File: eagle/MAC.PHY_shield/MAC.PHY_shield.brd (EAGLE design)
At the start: 49.9 x 49.9 mm, 23 parts, among them IC1 ENC28J60, Q1 CSM-7X-DU

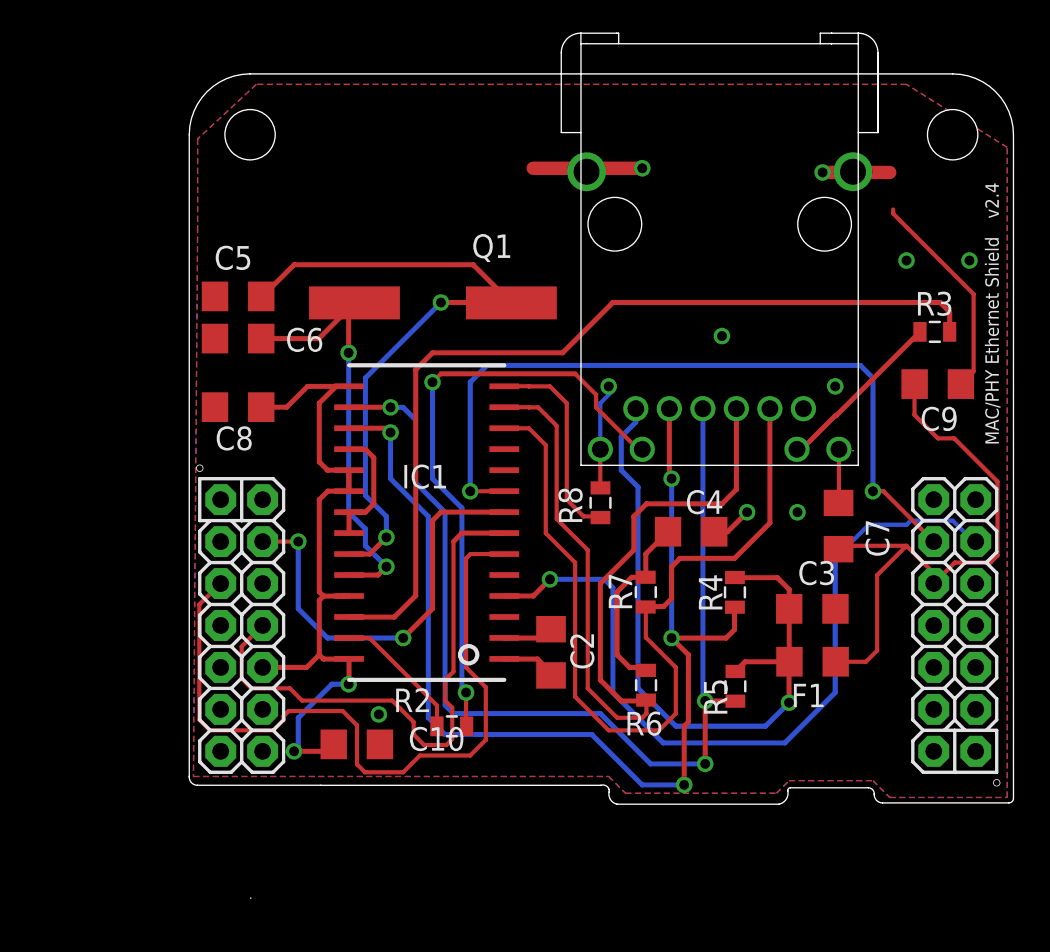
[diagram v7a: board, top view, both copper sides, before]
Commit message: Sent out boards to itead, last minute changes included.
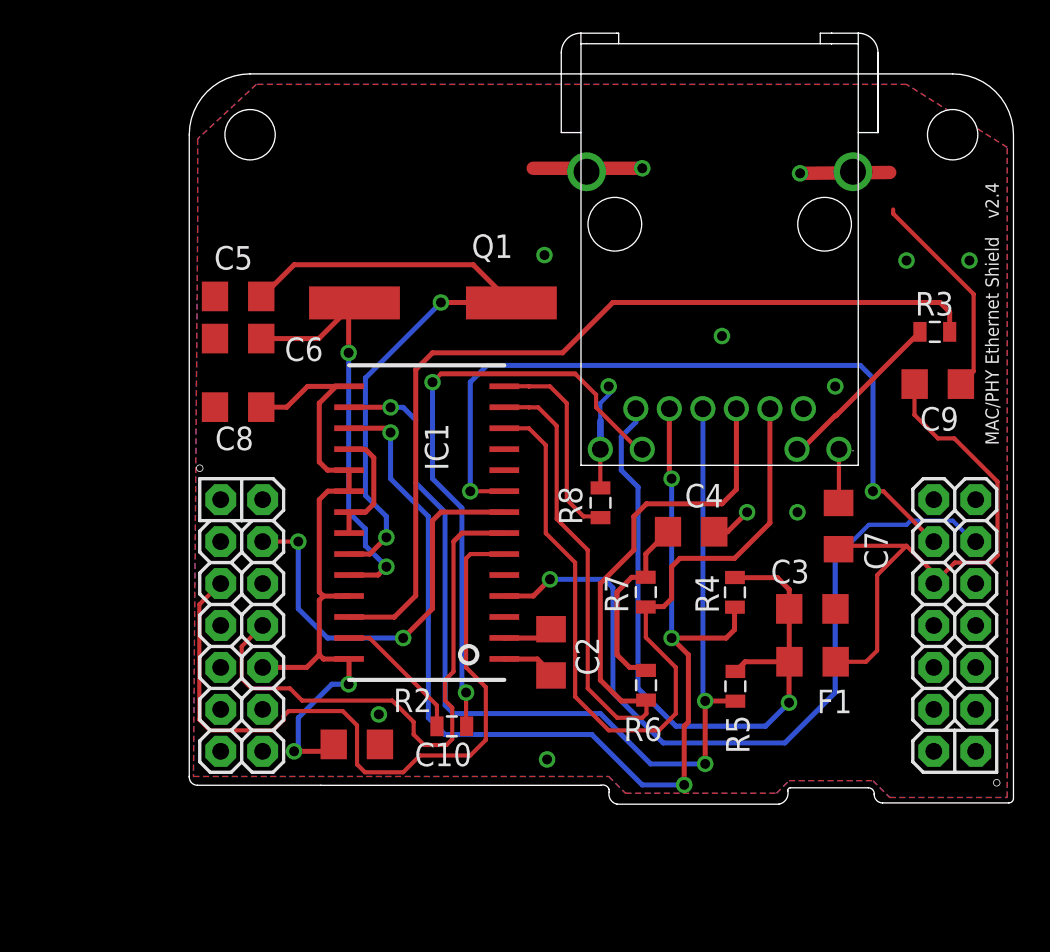
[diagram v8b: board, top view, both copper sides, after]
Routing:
- net GND: track 46.1 -> 49.2 mm, vias 10 -> 12
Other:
- board size 49.9 x 49.9 mm -> 49.9 x 44.2 mm
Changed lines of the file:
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@@
 <?xml version="1.0" encoding="utf-8"?>
 <!DOCTYPE eagle SYSTEM "eagle.dtd">
-<eagle version="6.1">
+<eagle version="6.3">
 <drawing>
 <settings>
@@
 <board>
 <plain>
-<wire x1="13.8684" y1="8.89" x2="13.8938" y2="8.89" width="0" layer="20"/>
 <wire x1="18.1356" y1="15.7226" x2="35.0774" y2="15.7226" width="0" layer="20"/>
 <wire x1="35.0774" y1="15.7226" x2="35.5854" y2="15.4686" width="0" layer="20" curve="-90"/>
@@
 </class>
 </classes>
-<designrules>
+<designrules name="default">
 <description language="de">&lt;b&gt;EAGLE Design Rules&lt;/b&gt;
 &lt;p&gt;
@@
 <element name="U$1" library="ASL" package="CANODE_SHIELD" value="CANODE_SHIELD" x="10.16" y="8.89" smashed="yes"/>
 <element name="IC1" library="ASL" package="SOIC28-W" value="ENC28J60" x="24.638" y="31.7754" smashed="yes" rot="R180">
-<attribute name="NAME" x="25.8725" y="35.1229" size="1.4224" layer="25" ratio="15" rot="R180"/>
-<attribute name="VALUE" x="28.73" y="11.9454" size="1.4224" layer="27" ratio="15" rot="R180"/>
+<attribute name="NAME" x="24.4271" y="37.6425" size="1.4224" layer="25" ratio="15" rot="R270"/>
+<attribute name="VALUE" x="24.4746" y="33" size="1.4224" layer="27" ratio="15" rot="R270"/>
 </element>
 <element name="U$3" library="ASL" package="08B0-1X1T-06-F" value="MAGJACK" x="35.052" y="36.068" smashed="yes"/>
 <element name="C2" library="ASL" package="1206" value="10uF" x="32.0675" y="23.7744" smashed="yes" rot="R90">
-<attribute name="NAME" x="34.671" y="22.6949" size="1.4224" layer="25" ratio="10" rot="R90"/>
+<attribute name="NAME" x="34.981" y="22.3649" size="1.4224" layer="25" ratio="10" rot="R90"/>
 </element>
 <element name="R2" library="ASL" package="0805" value="300" x="26.0604" y="19.2913" smashed="yes" rot="R180">
@@
 </element>
 <element name="R4" library="ASL" package="0805" value="49.9" x="43.2054" y="27.4066" smashed="yes" rot="R90">
-<attribute name="NAME" x="42.4434" y="26.2001" size="1.4224" layer="25" ratio="15" rot="R90"/>
+<attribute name="NAME" x="42.2334" y="26.1401" size="1.4224" layer="25" ratio="15" rot="R90"/>
 </element>
 <element name="R5" library="ASL" package="0805" value="49.9" x="43.2308" y="21.717" smashed="yes" rot="R270">
-<attribute name="NAME" x="41.3258" y="22.225" size="1.4224" layer="25" ratio="15" rot="R270"/>
+<attribute name="NAME" x="42.6658" y="19.975" size="1.4224" layer="25" ratio="15" rot="R270"/>
 </element>
 <element name="R6" library="ASL" package="0805" value="49.9" x="37.8206" y="21.7805" smashed="yes" rot="R90">
-<attribute name="NAME" x="38.862" y="20.1676" size="1.4224" layer="25" ratio="15" rot="R180"/>
+<attribute name="NAME" x="38.802" y="19.8276" size="1.4224" layer="25" ratio="15" rot="R180"/>
 </element>
 <element name="R7" library="ASL" package="0805" value="49.9" x="37.8079" y="27.4193" smashed="yes" rot="R270">
-<attribute name="NAME" x="36.9824" y="26.2763" size="1.4224" layer="25" ratio="15" rot="R90"/>
+<attribute name="NAME" x="36.7424" y="26.1563" size="1.4224" layer="25" ratio="15" rot="R90"/>
 </element>
 <element name="F1" library="ASL" package="1206" value="FERRITE_BEAD" x="47.9044" y="23.2029" smashed="yes" rot="R180">
-<attribute name="NAME" x="48.7299" y="21.8694" size="1.4224" layer="25" ratio="10" rot="R180"/>
+<attribute name="NAME" x="50.2999" y="21.5094" size="1.4224" layer="25" ratio="10" rot="R180"/>
 </element>
 <element name="C3" library="ASL" package="1206" value=".1 uF" x="47.8917" y="26.4033" smashed="yes">
-<attribute name="NAME" x="47.0027" y="27.8638" size="1.4224" layer="25" ratio="10"/>
+<attribute name="NAME" x="45.3727" y="27.9538" size="1.4224" layer="25" ratio="10"/>
 </element>
 <element name="C4" library="ASL" package="1206" value=".1 uF" x="40.5511" y="31.0769" smashed="yes">
-<attribute name="NAME" x="40.1955" y="32.1564" size="1.4224" layer="25" ratio="10"/>
+<attribute name="NAME" x="40.1655" y="32.5464" size="1.4224" layer="25" ratio="10"/>
 </element>
 <element name="R8" library="ASL" package="0805" value="2.32 k" x="35.0647" y="32.8295" smashed="yes" rot="R270">
@@
 </element>
 <element name="C6" library="ASL" package="1206" value="33 pF" x="13.1191" y="42.7736" smashed="yes" rot="R180">
-<attribute name="NAME" x="18.3261" y="43.4086" size="1.4224" layer="25" ratio="10" rot="R180"/>
+<attribute name="NAME" x="18.2761" y="42.8386" size="1.4224" layer="25" ratio="10" rot="R180"/>
 </element>
 <element name="C7" library="ASL" package="1206" value=".1 uF" x="49.4792" y="31.4198" smashed="yes" rot="R270">
-<attribute name="NAME" x="51.1302" y="31.8643" size="1.4224" layer="25" ratio="10" rot="R270"/>
+<attribute name="NAME" x="51.0402" y="31.1043" size="1.4224" layer="25" ratio="10" rot="R270"/>
 </element>
 <element name="C8" library="ASL" package="1206" value=".1 uF" x="13.1191" y="38.6207" smashed="yes">
@@
 </element>
 <element name="C10" library="ASL" package="1206" value=".1 uF" x="20.3073" y="18.1991" smashed="yes">
-<attribute name="NAME" x="23.4188" y="17.8181" size="1.4224" layer="25" ratio="10"/>
+<attribute name="NAME" x="23.8088" y="16.8781" size="1.4224" layer="25" ratio="10"/>
 </element>
 <element name="E$3" library="ASL" package="STAND-OFF-TIGHT" value="" x="13.843" y="55.118" smashed="yes"/>
@@
 <wire x1="30.988" y1="53.086" x2="37.592" y2="53.086" width="0.8128" layer="1"/>
 <via x="37.592" y="53.086" extent="1-16" drill="0.6"/>
-<wire x1="48.514" y1="52.832" x2="52.578" y2="52.832" width="0.8128" layer="1"/>
-<via x="48.514" y="52.832" extent="1-16" drill="0.6"/>
+<wire x1="47.15" y1="52.78" x2="52.578" y2="52.832" width="0.8128" layer="1"/>
+<via x="47.15" y="52.78" extent="1-16" drill="0.6"/>
 <via x="42.418" y="42.926" extent="1-16" drill="0.6"/>
 <wire x1="35.052" y1="36.068" x2="35.052" y2="38.862" width="0.254" layer="16"/>
@@
 <via x="35.56" y="39.878" extent="1-16" drill="0.6"/>
 <via x="49.276" y="39.878" extent="1-16" drill="0.6"/>
-<wire x1="29.238" y1="36.0754" x2="35.052" y2="36.068" width="0" layer="19" extent="1-16"/>
+<via x="31.67" y="47.83" extent="1-16" drill="0.6" shape="square"/>
+<wire x1="35.052" y1="36.068" x2="35.06" y2="36.068" width="0.4064" layer="16"/>
+<wire x1="35.06" y1="36.068" x2="35.06" y2="37.8" width="0.4064" layer="16"/>
+<via x="31.83" y="17.29" extent="1-16" drill="0.6" shape="square"/>
 </signal>
 <signal name="N$1">
